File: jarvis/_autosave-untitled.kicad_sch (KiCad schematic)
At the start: 26 parts, among them IC3 MCP73871T-4CAI_ML, IC4 TLV70033DDCT, J3 Conn_01x02 - Battery, U1 TPD4E05U06QDQARQ1, U2 2137160001

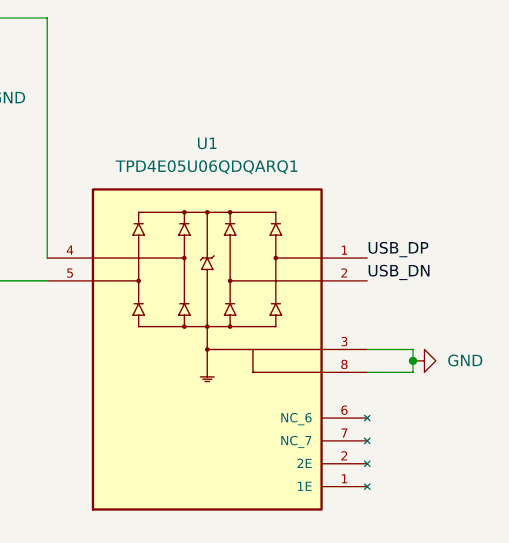
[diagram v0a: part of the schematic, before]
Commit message: small fixes from testing new pcb swap d lines connected pins on power ic that needed to be changed rbg led to be common anode
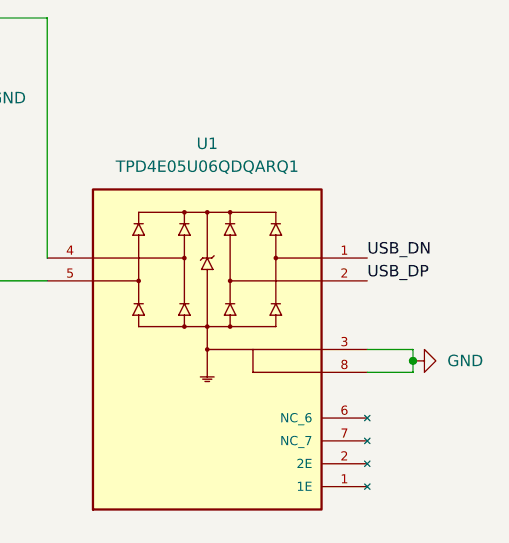
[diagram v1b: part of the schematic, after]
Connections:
- net USB_DN: now also U1.1 (1E); no longer U1.2 (2E)
- net USB_DP: now also U1.2 (2E); no longer U1.1 (1E)
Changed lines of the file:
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@@
 		)
 	)
-	(label "USB_DP"
+	(label "USB_DN"
 		(at 266.7 64.77 0)
 		(effects
@@
 		)
 	)
-	(label "USB_DN"
+	(label "USB_DP"
 		(at 266.7 67.31 0)
 		(effects
